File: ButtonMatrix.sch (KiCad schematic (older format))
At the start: 54 parts, among them SW201 SW_DPST, SW202 SW_DPST, SW203 SW_DPST, SW204 SW_DPST, SW205 SW_DPST, SW206 SW_DPST, SW207 SW_DPST, SW208 SW_DPST, SW209 SW_DPST, SW210 SW_DPST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

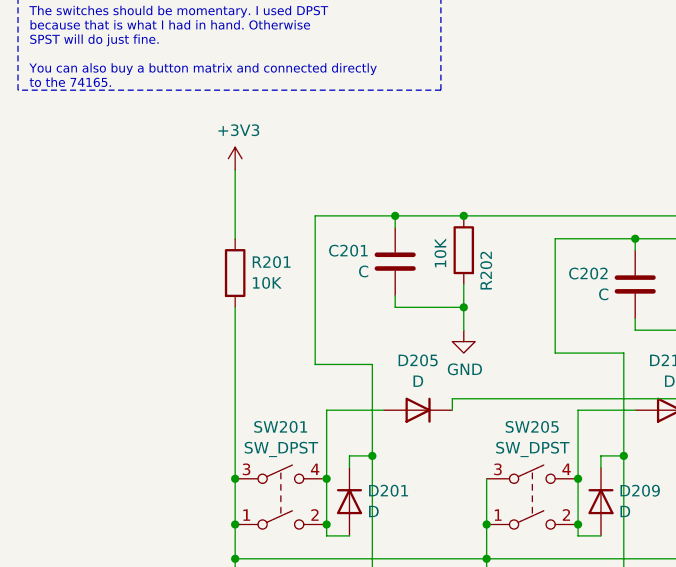
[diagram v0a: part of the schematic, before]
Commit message: Based on feedback, update silkscreen on DP101 and link to OSHPark, R201 from 10K to 1K.
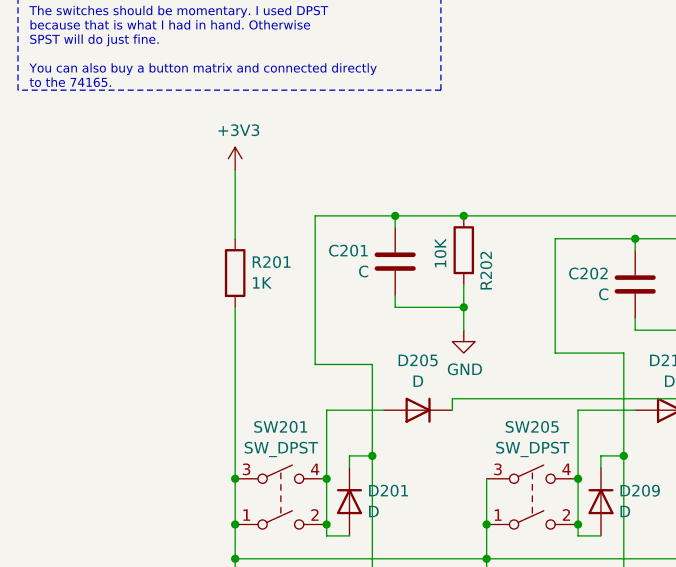
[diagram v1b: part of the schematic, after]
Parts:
- R201: value 10K -> 1K
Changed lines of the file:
@@
 P 1450 2250
 F 0 "R201" H 1520 2296 50  0000 L CNN
-F 1 "10K" H 1520 2205 50  0000 L CNN
+F 1 "1K" H 1520 2205 50  0000 L CNN
 F 2 "" V 1380 2250 50  0001 C CNN
 F 3 "~" H 1450 2250 50  0001 C CNN
